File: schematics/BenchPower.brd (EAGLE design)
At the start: 80 x 67 mm, 29 parts, among them U1 V_REG_317SINK, X2 9090-4R

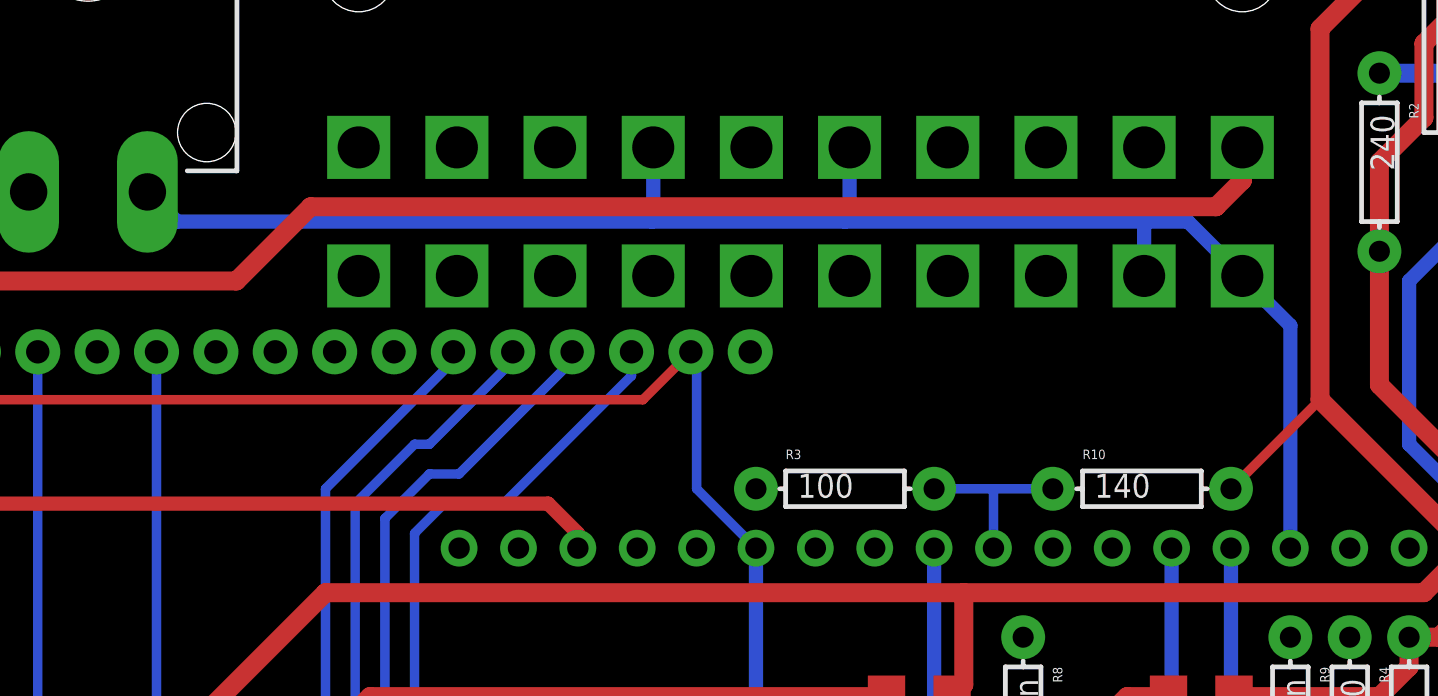
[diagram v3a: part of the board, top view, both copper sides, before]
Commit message: Adjust voltage sense software
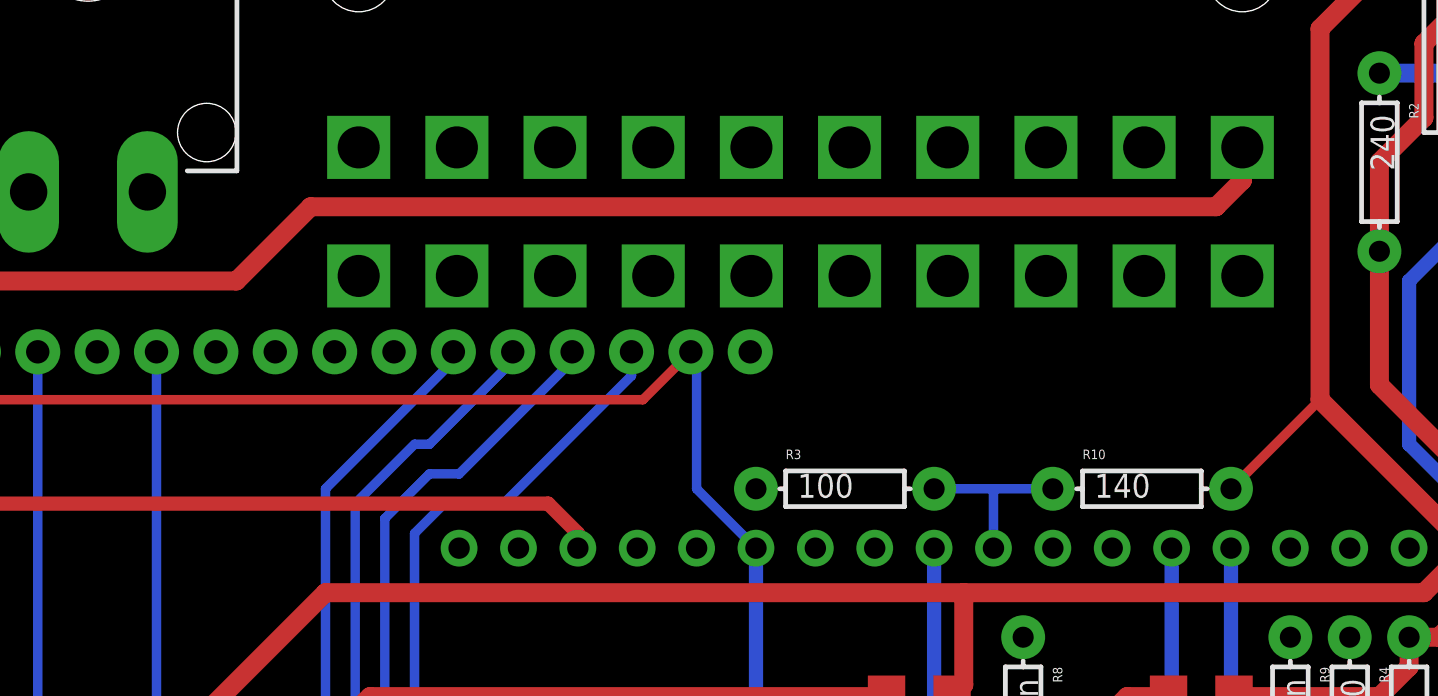
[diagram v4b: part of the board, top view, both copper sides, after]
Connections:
- removed net 5VHDR: U$1.P$19, U$1.P$20, U$1.P$4, U$1.P$6, U$2.P20, X2.4
- new net 5V$1: U$1.P$4
- new net 5V$2: U$1.P$6
- new net 5V$3: U$1.P$19
- new net 5V$4: U$1.P$20
- new net REF: U$2.P20
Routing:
- net 5VHDR: track 69.6 -> 0.00 mm
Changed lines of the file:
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@@
 <contactref element="U$1" pad="P$18"/>
-</signal>
-<signal name="5VHDR">
-<contactref element="U$1" pad="P$19"/>
-<contactref element="U$1" pad="P$20"/>
-<contactref element="U$1" pad="P$6"/>
-<contactref element="U$1" pad="P$4"/>
-<contactref element="X2" pad="4"/>
-<contactref element="U$2" pad="P20"/>
-<wire x1="20.32" y1="53.975" x2="21.59" y2="52.705" width="0.6096" layer="16"/>
-<wire x1="21.59" y1="52.705" x2="41.91" y2="52.705" width="0.6096" layer="16"/>
-<wire x1="41.91" y1="52.705" x2="50.165" y2="52.705" width="0.6096" layer="16"/>
-<wire x1="50.165" y1="52.705" x2="62.865" y2="52.705" width="0.6096" layer="16"/>
-<wire x1="62.865" y1="52.705" x2="64.835" y2="52.705" width="0.6096" layer="16"/>
-<wire x1="64.835" y1="52.705" x2="67.16" y2="50.38" width="0.6096" layer="16"/>
-<wire x1="41.96" y1="55.88" x2="41.96" y2="52.755" width="0.6096" layer="16"/>
-<wire x1="41.96" y1="52.755" x2="41.91" y2="52.705" width="0.6096" layer="16"/>
-<wire x1="50.36" y1="55.88" x2="50.36" y2="52.9" width="0.6096" layer="16"/>
-<wire x1="50.36" y1="52.9" x2="50.165" y2="52.705" width="0.6096" layer="16"/>
-<wire x1="62.96" y1="50.38" x2="62.96" y2="52.61" width="0.6096" layer="16"/>
-<wire x1="62.96" y1="52.61" x2="62.865" y2="52.705" width="0.6096" layer="16"/>
-<wire x1="67.16" y1="50.38" x2="67.16" y2="50.315" width="0.6096" layer="16"/>
-<wire x1="67.16" y1="50.315" x2="69.215" y2="48.26" width="0.6096" layer="16"/>
-<wire x1="69.215" y1="48.26" x2="69.215" y2="38.735" width="0.6096" layer="16"/>
 </signal>
 <signal name="3V3">
@@
 <wire x1="70.485" y1="45.085" x2="66.675" y2="41.275" width="0.4064" layer="1"/>
 </signal>
+<signal name="REF">
+<contactref element="U$2" pad="P20"/>
+</signal>
+<signal name="5V$1">
+<contactref element="U$1" pad="P$4"/>
+</signal>
+<signal name="5V$2">
+<contactref element="U$1" pad="P$6"/>
+</signal>
+<signal name="5V$3">
+<contactref element="U$1" pad="P$19"/>
+</signal>
+<signal name="5V$4">
+<contactref element="U$1" pad="P$20"/>
+</signal>
 </signals>

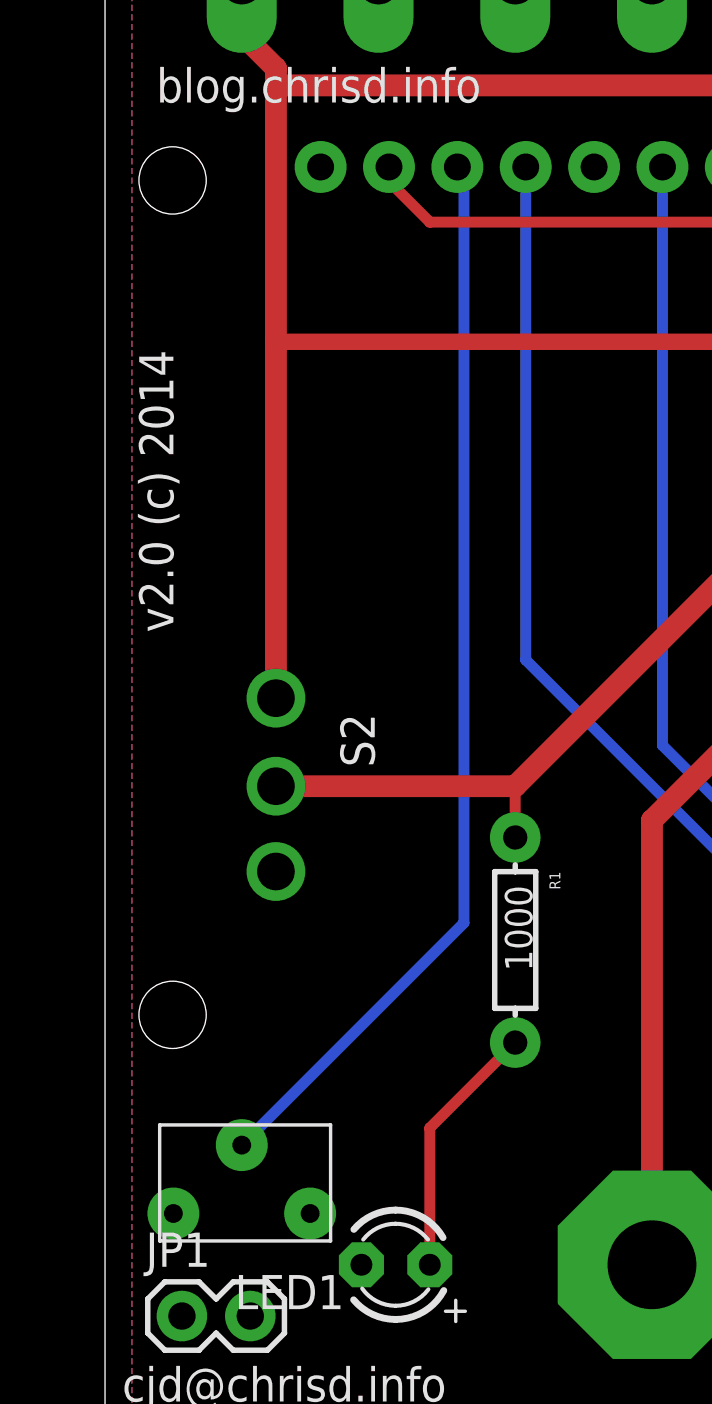
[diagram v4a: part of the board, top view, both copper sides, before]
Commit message: Small routing change for trimpot
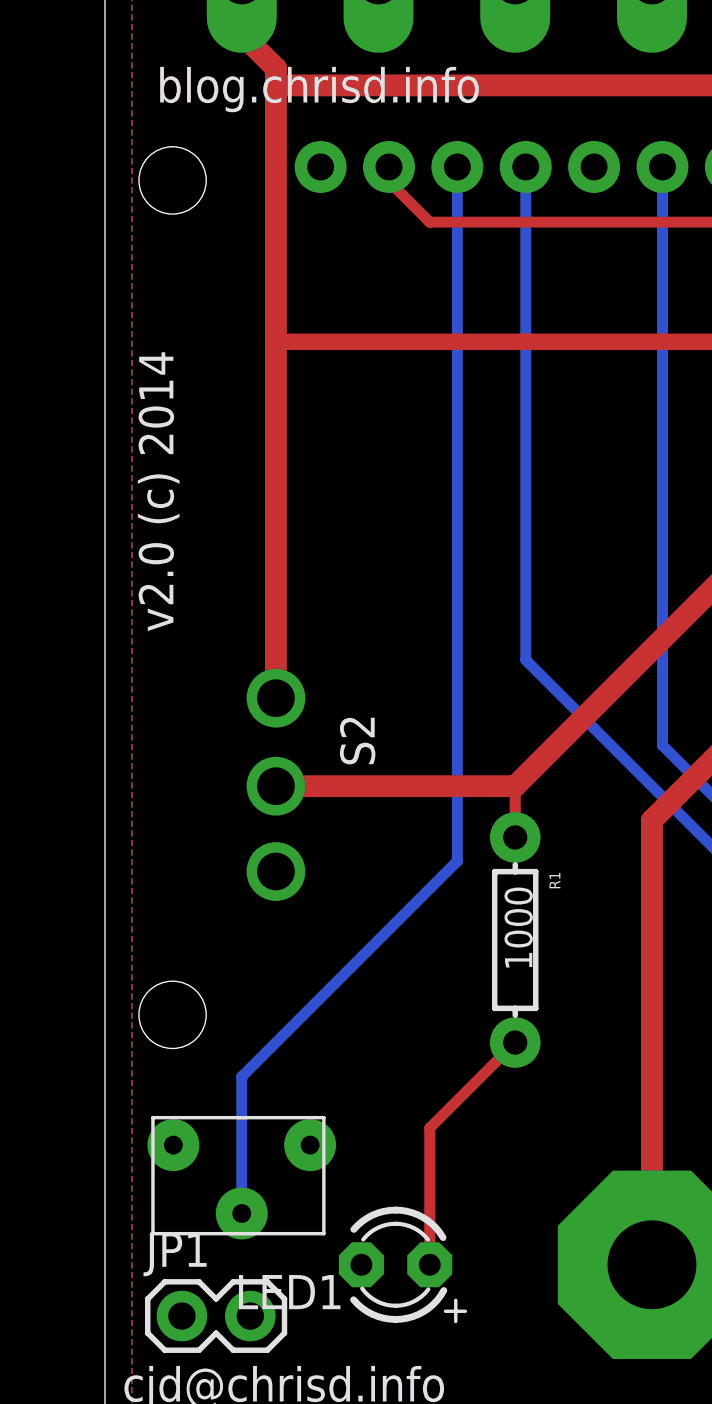
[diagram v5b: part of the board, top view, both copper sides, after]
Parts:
- moved RV1 5.68 mm to (2.54, 10.8), turned to 0 degrees
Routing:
- net LCD_CONTRAST: track 39.9 -> 42.2 mm
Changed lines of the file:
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@@
 <element name="R4" library="SparkFun-Passives" package="AXIAL-0.3" value="100" x="71.755" y="31.115" rot="R270"/>
 <element name="R5" library="SparkFun-Passives" package="AXIAL-0.3" value="140" x="74.295" y="31.115" rot="R90"/>
-<element name="RV1" library="desjardins" package="3266W" value="" x="7.62" y="8.255" rot="R180"/>
+<element name="RV1" library="desjardins" package="3266W" value="" x="2.54" y="10.795"/>
 <element name="JP1" library="SparkFun-Connectors" package="1X02" value="M02PTH" x="2.8575" y="4.445"/>
 <element name="JP4" library="SparkFun-Connectors" package="1X02" value="M02PTH" x="48.5775" y="4.445"/>
@@
 <contactref element="U$4" pad="P$3"/>
 <contactref element="RV1" pad="P$2"/>
-<wire x1="13.335" y1="19.05" x2="13.335" y2="46.89" width="0.4064" layer="16"/>
-<wire x1="13.335" y1="46.89" x2="13.09" y2="47.135" width="0.4064" layer="16"/>
-<wire x1="13.335" y1="19.05" x2="5.08" y2="10.795" width="0.4064" layer="16"/>
+<wire x1="13.09" y1="47.135" x2="13.09" y2="21.345" width="0.4064" layer="16"/>
+<wire x1="13.09" y1="21.345" x2="5.08" y2="13.335" width="0.4064" layer="16"/>
+<wire x1="5.08" y1="13.335" x2="5.08" y2="8.255" width="0.4064" layer="16"/>
 </signal>
 <signal name="12VHDRTAP">

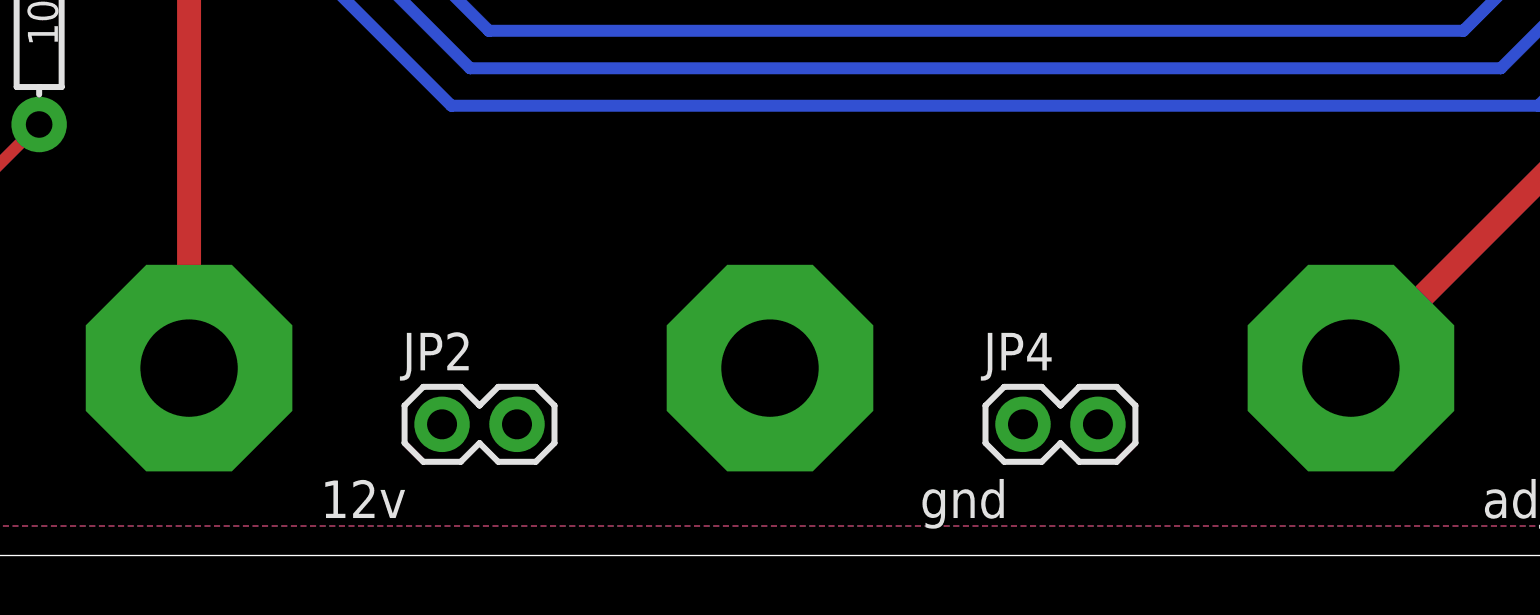
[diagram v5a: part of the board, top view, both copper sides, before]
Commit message: Adding new headers for jumper wires
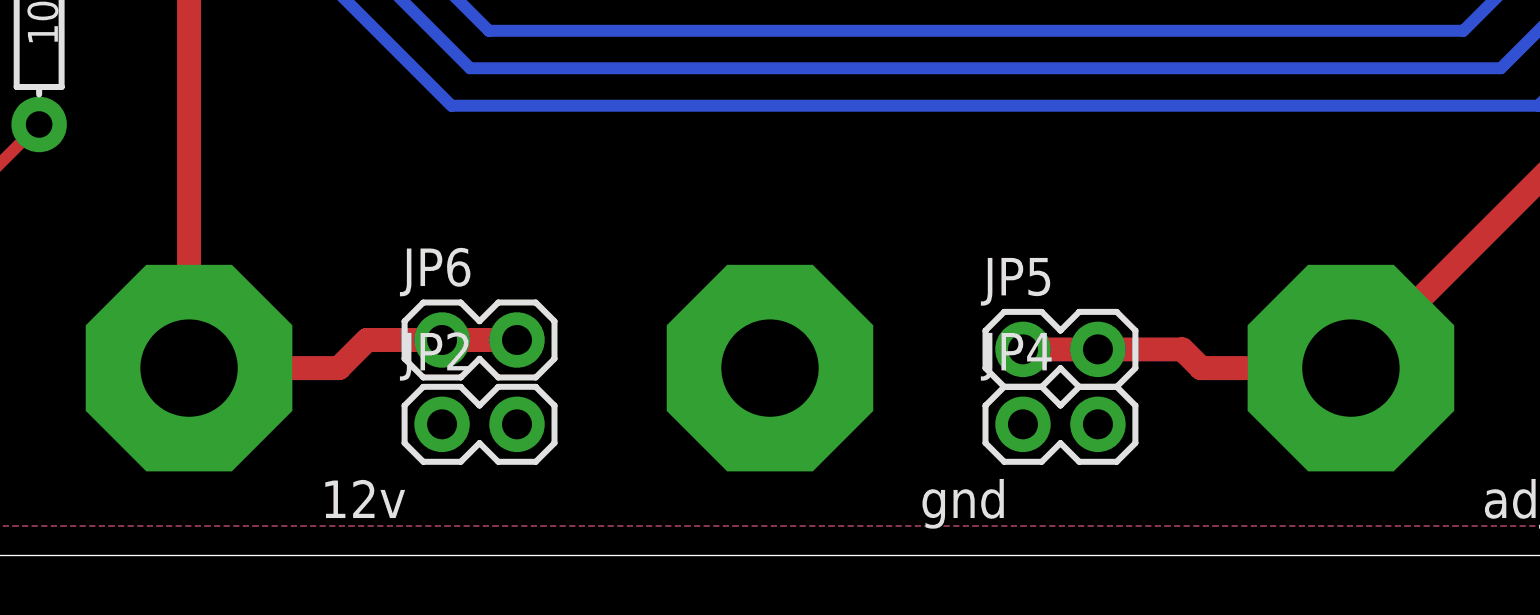
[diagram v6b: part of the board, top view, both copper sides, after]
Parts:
- added JP5, JP6: M02PTH, SparkFun-Connectors:1X02
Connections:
- net AMPS12VHDR: now also JP6.1, JP6.2
- net AMPS12VREG: now also JP5.1, JP5.2
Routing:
- net AMPS12VHDR: track 55.0 -> 66.5 mm
- net AMPS12VREG: track 52.7 -> 64.1 mm
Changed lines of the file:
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@@
 <?xml version="1.0" encoding="utf-8"?>
 <!DOCTYPE eagle SYSTEM "eagle.dtd">
-<eagle version="6.5.0">
+<eagle version="7.0.0">
 <drawing>
 <settings>
@@
 <setting verticaltext="up"/>
 </settings>
-<grid distance="0.025" unitdist="inch" unit="inch" style="lines" multiple="1" display="yes" altdistance="0.025" altunitdist="inch" altunit="inch"/>
+<grid distance="0.0125" unitdist="inch" unit="inch" style="lines" multiple="1" display="yes" altdistance="0.025" altunitdist="inch" altunit="inch"/>
 <layers>
 <layer number="1" name="Top" color="4" fill="1" visible="yes" active="yes"/>
@@
 <pass name="Default">
 <param name="RoutingGrid" value="50mil"/>
+<param name="AutoGrid" value="1"/>
+<param name="Efforts" value="0"/>
+<param name="TopRouterVariant" value="1"/>
 <param name="tpViaShape" value="round"/>
 <param name="PrefDir.1" value="|"/>
@@
 <element name="RV1" library="desjardins" package="3266W" value="" x="2.54" y="10.795"/>
 <element name="JP1" library="SparkFun-Connectors" package="1X02" value="M02PTH" x="2.8575" y="4.445"/>
-<element name="JP4" library="SparkFun-Connectors" package="1X02" value="M02PTH" x="48.5775" y="4.445"/>
 <element name="U5" library="SparkFun-AnalogIC" package="SOT23-5" value="" x="53.34" y="28.575" rot="R90"/>
 <element name="U6" library="SparkFun-AnalogIC" package="SOT23-5" value="" x="65.405" y="28.575" rot="R90"/>
@@
 <element name="S2" library="desjardins" package="EG1213" value="EG1213" x="6.35" y="24.13" rot="R270"/>
 <element name="JP2" library="SparkFun-Connectors" package="1X02" value="M02PTH" x="28.8925" y="4.445"/>
-<element name="JP3" library="SparkFun-Connectors" package="1X02" value="M02PTH" x="74.93" y="11.43"/>
 <element name="R3" library="SparkFun-Passives" package="AXIAL-0.3" value="100" x="50.165" y="41.275"/>
 <element name="R10" library="SparkFun-Passives" package="AXIAL-0.3" value="140" x="62.865" y="41.275"/>
+<element name="JP3" library="SparkFun-Connectors" package="1X02" value="M02PTH" x="74.93" y="11.43"/>
+<element name="JP4" library="SparkFun-Connectors" package="1X02" value="M02PTH" x="48.5775" y="4.445"/>
+<element name="JP5" library="SparkFun-Connectors" package="1X02" value="M02PTH" x="48.5775" y="6.985"/>
+<element name="JP6" library="SparkFun-Connectors" package="1X02" value="M02PTH" x="28.8925" y="7.3025"/>
 </elements>
 <signals>
@@
 <contactref element="JP1" pad="2"/>
 <contactref element="JP1" pad="1"/>
+<contactref element="R3" pad="P$1"/>
+<contactref element="JP4" pad="1"/>
+<contactref element="JP4" pad="2"/>
+<contactref element="JP3" pad="1"/>
+<contactref element="JP3" pad="2"/>
+<contactref element="JP2" pad="1"/>
 <contactref element="JP2" pad="2"/>
-<contactref element="JP2" pad="1"/>
-<contactref element="JP3" pad="2"/>
-<contactref element="JP3" pad="1"/>
-<contactref element="JP4" pad="2"/>
-<contactref element="JP4" pad="1"/>
-<contactref element="R3" pad="P$1"/>
 </signal>
 <signal name="5VSB">
@@
 <wire x1="60.325" y1="26.67" x2="61.595" y2="25.4" width="0.8128" layer="1"/>
 <wire x1="61.595" y1="25.4" x2="74.93" y2="25.4" width="0.8128" layer="1"/>
+<contactref element="JP5" pad="2"/>
+<contactref element="JP5" pad="1"/>
+<wire x1="59.69" y1="6.35" x2="54.61" y2="6.35" width="0.8128" layer="1"/>
+<wire x1="54.61" y1="6.35" x2="53.975" y2="6.985" width="0.8128" layer="1"/>
+<wire x1="53.975" y1="6.985" x2="51.1175" y2="6.985" width="0.8128" layer="1"/>
+<wire x1="51.1175" y1="6.985" x2="48.5775" y2="6.985" width="0.8128" layer="1"/>
 </signal>
 <signal name="AMPS12VHDR">
@@
 <wire x1="20.32" y1="22.86" x2="29.845" y2="32.385" width="0.8128" layer="1"/>
 <wire x1="29.845" y1="32.385" x2="51.94" y2="32.385" width="0.8128" layer="1"/>
+<contactref element="JP6" pad="2"/>
+<contactref element="JP6" pad="1"/>
+<wire x1="20.32" y1="6.35" x2="25.4" y2="6.35" width="0.8128" layer="1"/>
+<wire x1="25.4" y1="6.35" x2="26.3525" y2="7.3025" width="0.8128" layer="1"/>
+<wire x1="26.3525" y1="7.3025" x2="28.8925" y2="7.3025" width="0.8128" layer="1"/>
+<wire x1="28.8925" y1="7.3025" x2="31.4325" y2="7.3025" width="0.8128" layer="1"/>
 </signal>
 <signal name="3.3V$2">
